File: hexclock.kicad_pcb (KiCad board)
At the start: 2 copper layers, 60 x 52 mm, 40 parts, among them J1 USB_B_Micro, U1 MCP7940N-xSN, U2 ATtiny88-MU, Y1 7pF CL

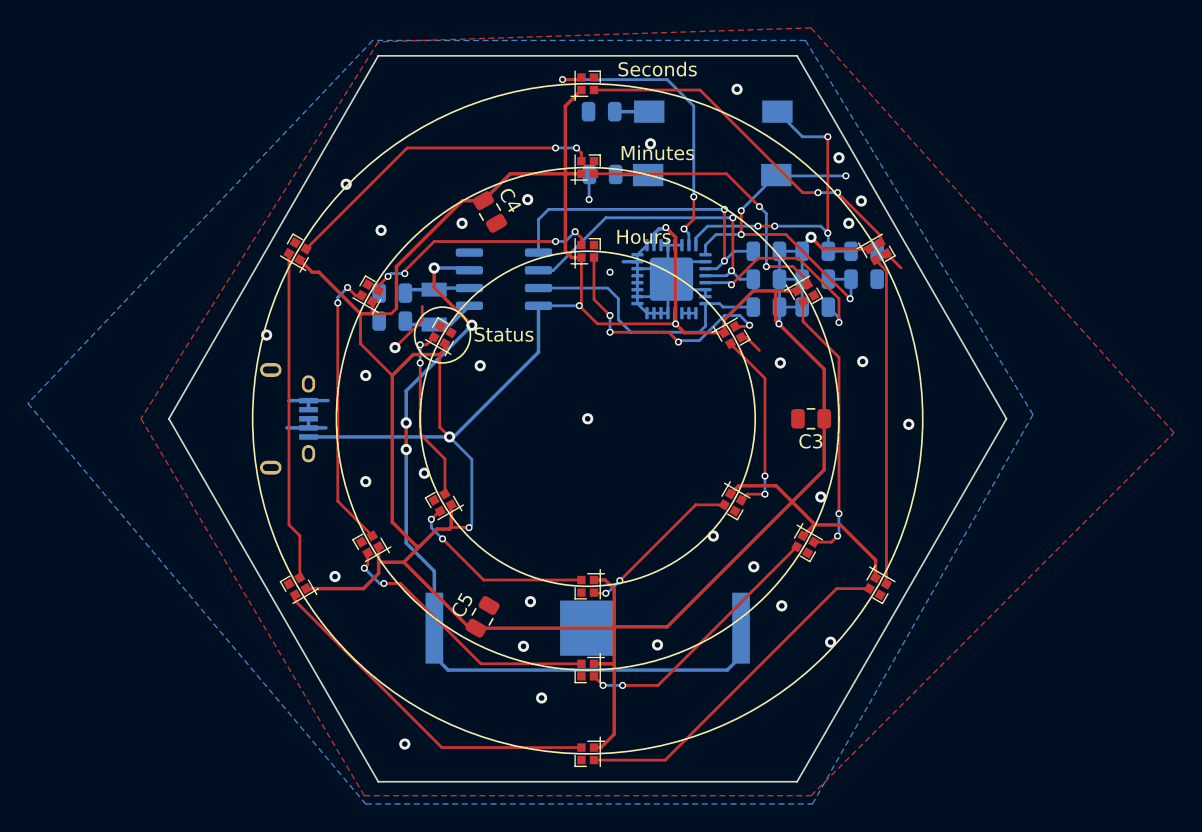
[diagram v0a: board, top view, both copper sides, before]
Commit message: Switch to using oscillator; update version
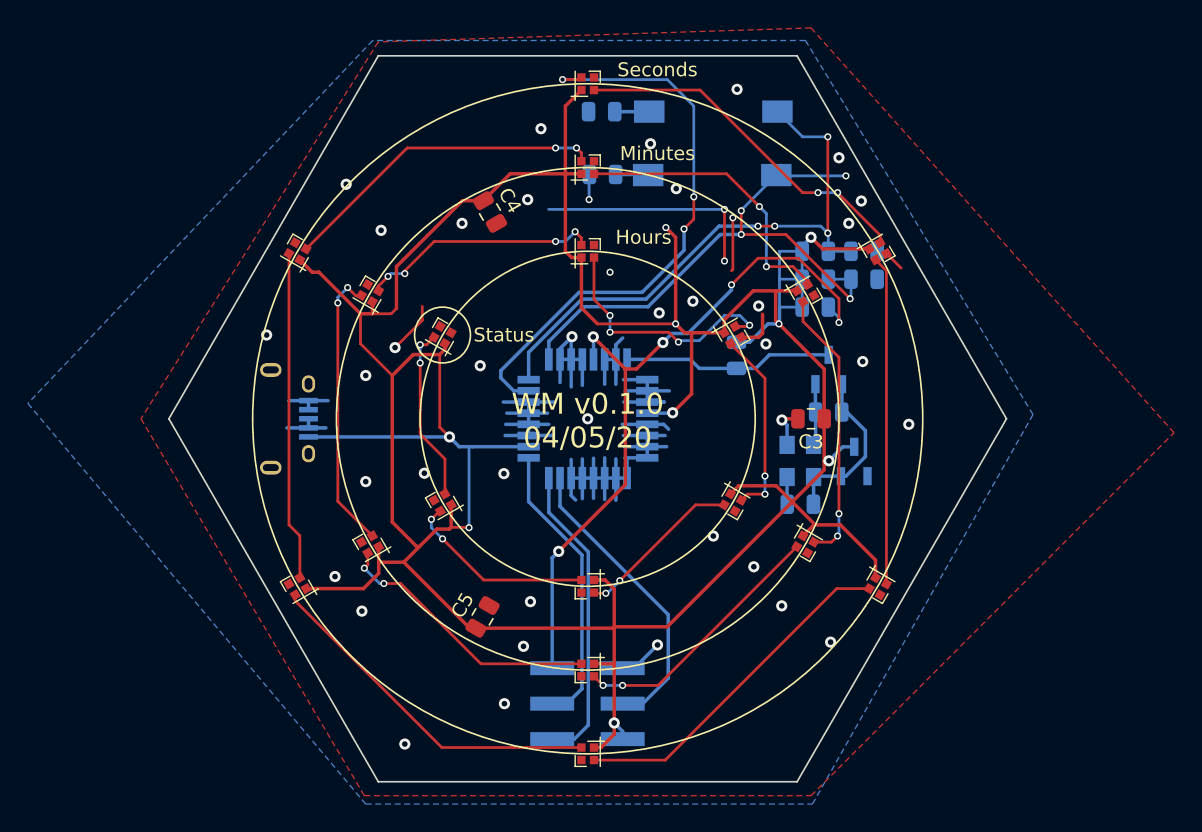
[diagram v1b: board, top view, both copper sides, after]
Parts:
- removed BT1: Battery_Cell, Battery:BatteryHolder_Keystone_3034_1x20mm
- removed C1, C2: 8pF, Capacitor_SMD:C_0805_2012Metric
- removed Y1: 7pF CL, Crystal:Crystal_SMD_3215-2Pin_3.2x1.5mm
- added J2: AVR-ISP-6, Connector_PinHeader_2.54mm:PinHeader_2x03_P2.54mm_Vertical_SMD, B.Cu at (190.0, 85.4)
- added Q1: BSS138-7-F, digikey-footprints:SOT-23-3, B.Cu at (207.3, 61.5)
- added X1: ECS-327TXO, Oscillator:ECS-327MVATX-3, B.Cu at (205.2, 68.0)
- R2, R3: value 4.7kR -> 10kR
- R8: value 20kR -> 10kR
- U1: value MCP7940N-xSN -> MCP1700T-3302E_TT; footprint Package_SO:SOIC-8_3.9x4.9mm_P1.27mm -> digikey-footprints:SOT-23-3
- U2: footprint Package_DFN_QFN:QFN-32-1EP_5x5mm_P0.5mm_EP3.1x3.1mm -> Package_QFP:TQFP-32_7x7mm_P0.8mm
- moved U1 28.3 mm to (209.1, 68.1), turned to 90 degrees
- moved R2 18.3 mm to (205.2, 71.1)
- moved U2 11.7 mm to (190.0, 65.0), turned to 180 degrees
- moved R8 8.74 mm to (207.3, 64.5)
- moved R3 5.86 mm to (200.7, 60.5), turned to 270 degrees
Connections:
- net Net-(R1-Pad2) renamed RST
- R2 pad 1: +5V -> +3.3V
- R2 pad 2: SDA -> Net-(R2-Pad2)
- R3 pad 2: SCL -> SINT
- R8 pad 1: +5V -> +3.3V
- R8 pad 2: SINT -> USIT
- U1 pad 1: Net-(C1-Pad2) -> GND
- U1 pad 2: Net-(C2-Pad2) -> +3.3V
- U1 pad 3: VBAT -> +5V
- U2 pad 15: GND -> MOSI
- U2 pad 16: GND -> MISO
- U2 pad 17: GND -> SCK
- U2 pad 27: SDA -> GND
- U2 pad 28: SCL -> GND
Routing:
- net GND: track 43.1 -> 118.8 mm, vias 32 -> 43
- net VBAT: track 59.1 -> 0.00 mm, vias 4 -> 0
- net RST: track 14.7 -> 51.7 mm, vias 2 -> 5
- net SDA: track 23.6 -> 0.00 mm, vias 2 -> 0
- net SCL: track 23.2 -> 0.00 mm, vias 2 -> 0
- net MISO: track 0.00 -> 21.9 mm
- net MOSI: track 0.00 -> 21.6 mm
- net SCK: track 0.00 -> 20.7 mm
- net DOUT: track 22.0 -> 41.8 mm
- net HH: track 24.7 -> 41.5 mm
- net MM: track 27.8 -> 42.4 mm
- net +3.3V: track 0.00 -> 12.4 mm
- net Net-(C1-Pad2): track 5.25 -> 0.00 mm
- net Net-(C2-Pad2): track 4.74 -> 0.00 mm
- net SINT: track 19.7 -> 15.1 mm
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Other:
- board text added: "WM v0.1.0 04/05/20"
- board text removed: "WM v0.0.0 04/05/20"

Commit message: Optimize ground plane + vias
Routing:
- net GND: track 118.8 -> 98.6 mm, vias 43 -> 48
- net +5V: track 256.5 -> 249.1 mm, vias 9 -> 7

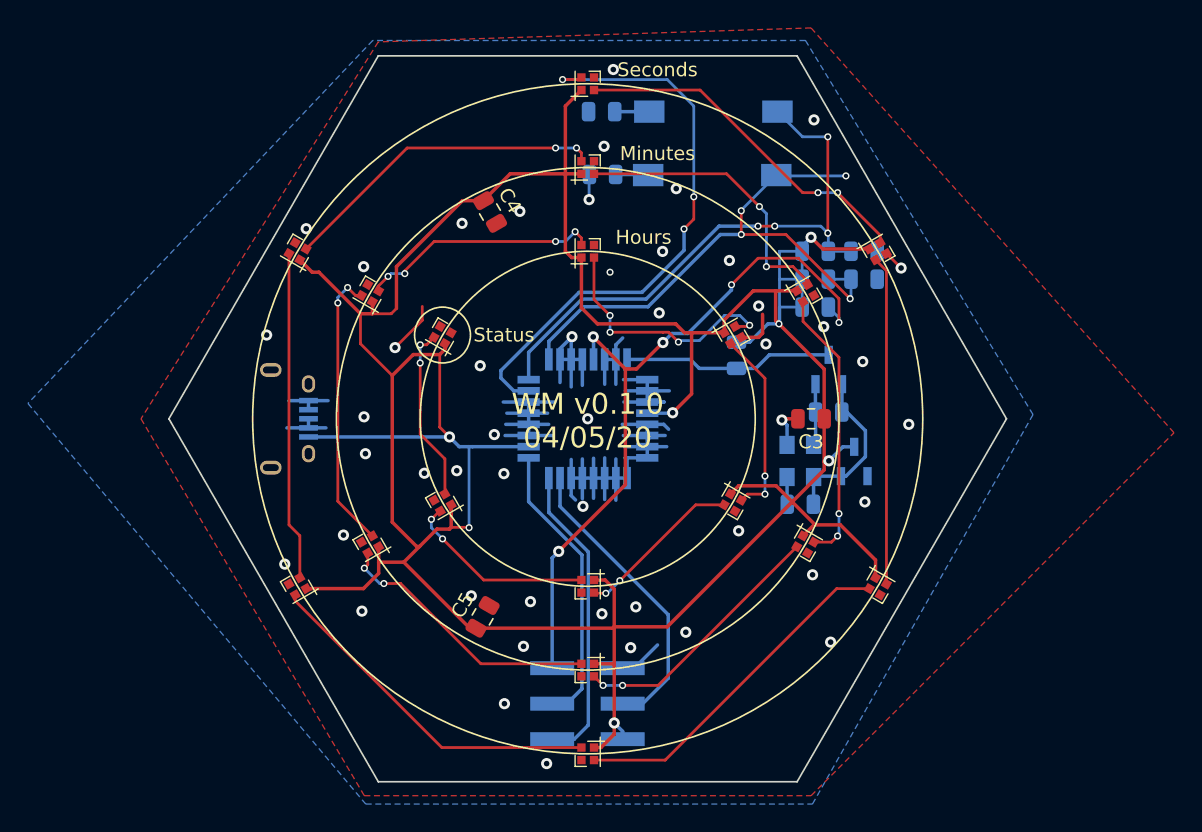
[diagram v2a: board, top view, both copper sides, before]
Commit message: Change time mech to RTC
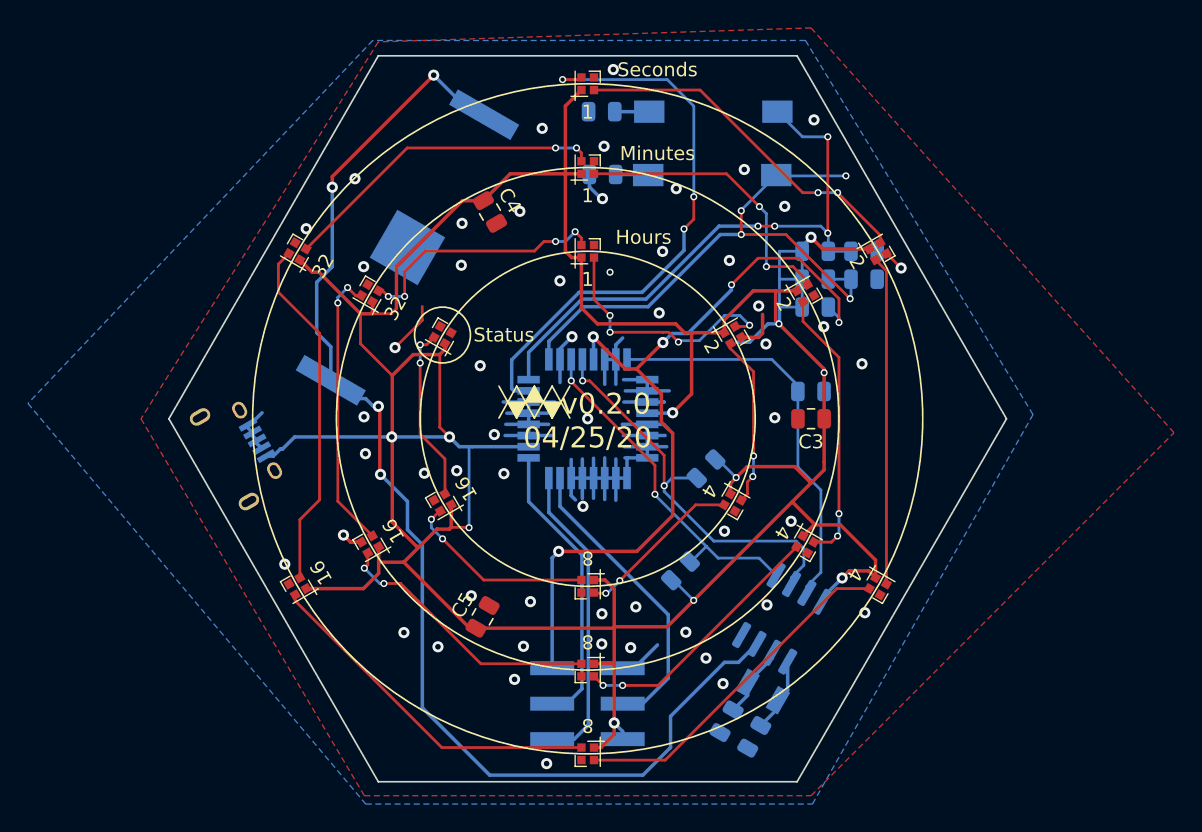
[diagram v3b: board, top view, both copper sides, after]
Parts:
- removed Q1: BSS138-7-F, digikey-footprints:SOT-23-3
- removed X1: ECS-327TXO, Oscillator:ECS-327MVATX-3
- added BT1: Battery_Cell, Battery:BatteryHolder_Keystone_3034_1x20mm, B.Cu at (177.1, 52.7)
- added C1: 8pF, Capacitor_SMD:C_0805_2012Metric, B.Cu at (201.9, 87.8)
- added C2: 8pF, Capacitor_SMD:C_0805_2012Metric, B.Cu at (199.9, 86.7)
- added REF**: Logo_WM, Symbol:Logo_WM, F.Cu at (186.2, 63.8)
- added Y1: 7pF CL, Crystal:Crystal_SMD_3215-2Pin_3.2x1.5mm, B.Cu at (202.5, 84.5)
- R2, R3, R8: value 10kR -> 1kR
- U1: value MCP1700T-3302E_TT -> MCP7940N-xSN; footprint digikey-footprints:SOT-23-3 -> Package_SO:SOIC-8_3.9x4.9mm_P1.27mm
- moved R3 16.0 mm to (196.6, 75.9), turned to 45 degrees
- moved U1 12.4 mm to (203.9, 79.3), turned to 60 degrees
- moved R2 7.22 mm to (198.5, 68.6), turned to 225 degrees
- moved J1 3.99 mm to (166.3, 66.5), turned to 120 degrees
- moved R8 1.95 mm to (206.0, 63.0)
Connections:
- R2 pad 1: +3.3V -> +5V
- R2 pad 2: Net-(R2-Pad2) -> SCL
- R3 pad 2: SINT -> SDA
- R8 pad 1: +3.3V -> +5V
- R8 pad 2: USIT -> MFP
- U1 pad 1: GND -> Net-(C1-Pad2)
- U1 pad 2: +3.3V -> Net-(C2-Pad2)
- U1 pad 3: +5V -> Net-(BT1-Pad1)
- U2 pad 27: GND -> SDA
- U2 pad 28: GND -> SCL
- U2 pad 32: SINT -> MFP
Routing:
- net Net-(BT1-Pad1): track 0.00 -> 88.8 mm, vias 0 -> 4
- net SCL: track 0.00 -> 29.3 mm, vias 0 -> 2
- net MFP: track 0.00 -> 29.0 mm
- net SDA: track 0.00 -> 24.9 mm, vias 0 -> 2
- net SINT: track 15.1 -> 0.00 mm
- net +5V: track 249.1 -> 263.2 mm, vias 7 -> 11
- net +3.3V: track 12.4 -> 0.00 mm
- net GND: track 98.6 -> 86.9 mm, vias 48 -> 55
- net RST: track 51.7 -> 57.5 mm
- net Net-(C1-Pad2): track 0.00 -> 5.37 mm
- net Net-(C2-Pad2): track 0.00 -> 5.26 mm
- net USIT: track 4.42 -> 0.00 mm
- net Net-(R2-Pad2): track 1.95 -> 0.00 mm
- net Net-(D5-Pad1): track 23.5 -> 25.3 mm
- net Net-(D14-Pad1): track 13.7 -> 12.3 mm
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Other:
- board text added: "+5V"
- board text added: "1"
- board text added: "16"
- board text added: "2"
- board text added: "32"
- board text added: "4"
- board text added: "8"
- board text added: "GND"
- board text added: "MISO"
- board text added: "MOSI"
- board text added: "RST"
- board text added: "SCK"
- board text added: "v0.2.0 04/25/20"
- board text removed: "WM v0.1.0 04/05/20"
